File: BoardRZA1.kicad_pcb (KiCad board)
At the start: 4 copper layers, 85.5 x 79.9 mm, 158 parts, among them CON1 USB-MINI-B, CON2 USB-A-PCB, CON3 microSD, CON4 BARREL_JACK, J1 VGA, J2 SUPP32, K1 CONN_3, P1 CONN_5X2, P10 CONN_1, P11 CONN_1, P12 CONN_1, P13 CONN_1, P14 CONN_1, P15 CONN_1, P16 CONN_1, P17 CONN_1, P2 CONN_1, P3 CONN_1, P4 CONN_1, P5 CONN_1, P6 CONN_1, P7 CONN_1, P8 CONN_1, P9 CONN_1, SW1 RESET, SW2 NMI, SW3 SW0, SW4 SW1, U1 RZ-A1L, U2 13MHz, U3 48MHz, U4 N25QXXX, U5 AS4C16M16S, U6 BA3259HFP, U7 BU42xx, U8 TL074, X1 32.768k

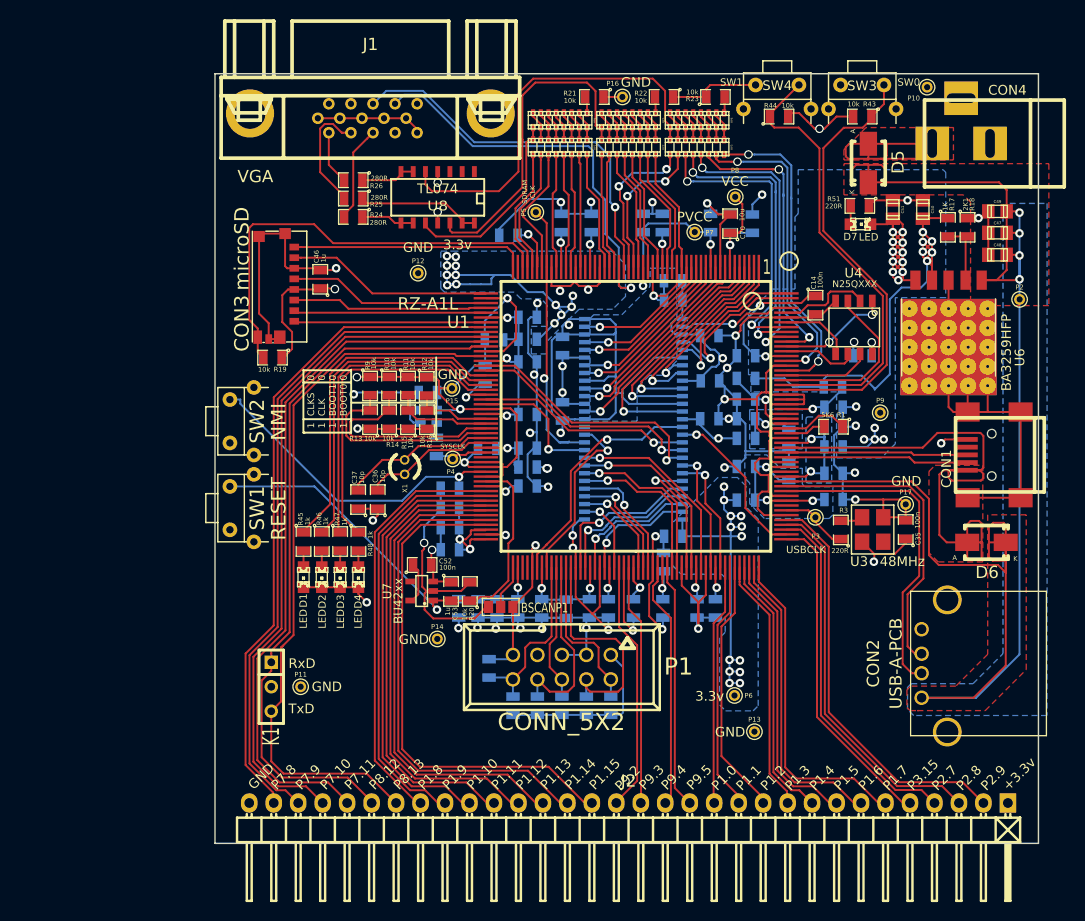
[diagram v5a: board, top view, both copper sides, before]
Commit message: Change R2R DAC for ADV7125 on LQFP48
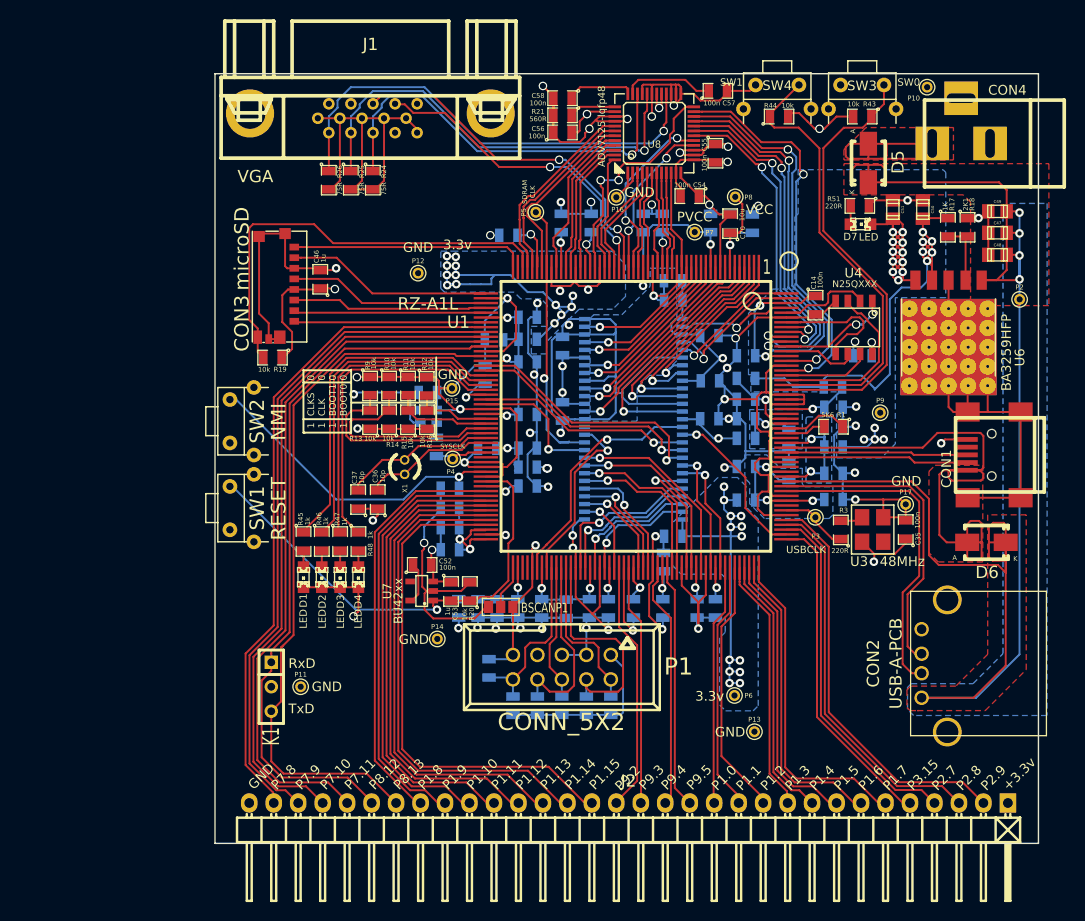
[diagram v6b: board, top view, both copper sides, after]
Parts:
- removed R22, R23: 10k, footprints:SM0805
- removed RP1, RP2, RP3: 20k, Resistors_SMD:r_cat16-8
- removed RP4, RP5, RP6: 10k, Resistors_SMD:r_cat16-8
- added C54: 100n, footprints:SM0805, F.Cu at (83.7, 30.4)
- added C55: 100n, footprints:SM0805, F.Cu at (86.4, 25.9)
- added C56: 100n, footprints:SM0805, F.Cu at (70.5, 23.7)
- added C57: 100n, footprints:SM0805, F.Cu at (86.6, 19.4)
- added C58: 100n, footprints:SM0805, F.Cu at (70.5, 20.2)
- R21: value 10k -> 560R
- R24, R25, R26: value 280R -> 75R
- U8: value TL074 -> ADV7125-lqfp48; footprint SMD_Packages:SO14E -> Housings_QFP:lqfp-48
- moved U8 23.5 mm to (80.0, 23.8), turned to 0 degrees
- moved P16 10.4 mm to (76.1, 30.5)
- moved R24 4.32 mm to (50.8, 28.7), turned to 270 degrees
- moved R21 3.81 mm to (70.5, 22.0)
- moved R26 2.54 mm to (46.2, 28.7), turned to 270 degrees
- moved R25 1.92 mm to (48.5, 28.7), turned to 270 degrees
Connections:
- J1 pad 1: Net-(J1-Pad1) -> /VGAB
- J1 pad 2: Net-(J1-Pad2) -> /VGAG
- J1 pad 3: Net-(J1-Pad3) -> /VGAR
- R21 pad 1: VSS -> Net-(R21-Pad1)
- R21 pad 2: Net-(R21-Pad2) -> VSS
- R24 pad 1: Net-(R24-Pad1) -> /VGAR
- R24 pad 2: Net-(J1-Pad3) -> VSS
- R25 pad 1: Net-(R25-Pad1) -> /VGAG
- R25 pad 2: Net-(J1-Pad2) -> VSS
- R26 pad 1: Net-(R26-Pad1) -> /VGAB
- R26 pad 2: Net-(J1-Pad1) -> VSS
- U1 pad 35: (no net) -> /LCD_PCLK
- U8 pad 1: (no net) -> VSS
- U8 pad 10: /VGA_B -> /LCD_DATA8
- U8 pad 11: VSS -> +3.3V
- U8 pad 12: /VGA_G -> VSS
- U8 pad 13: Net-(R25-Pad1) -> +3.3V
- U8 pad 14: Net-(R25-Pad1) -> VSS
- U8 pad 2: (no net) -> VSS
- U8 pad 3: (no net) -> /LCD_DATA15
- U8 pad 4: +3.3V -> /LCD_DATA14
- U8 pad 5: /VGA_R -> /LCD_DATA13
- U8 pad 6: Net-(R26-Pad1) -> /LCD_DATA12
- U8 pad 7: Net-(R26-Pad1) -> /LCD_DATA11
- U8 pad 8: Net-(R24-Pad1) -> /LCD_DATA10
- U8 pad 9: Net-(R24-Pad1) -> /LCD_DATA9
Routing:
- net VSS: track 566.0 -> 636.9 mm, vias 49 -> 56
- net /VGAB: track 0.00 -> 49.1 mm, vias 0 -> 1
- net /VGAG: track 0.00 -> 46.0 mm, vias 0 -> 1
- net /VGAR: track 0.00 -> 42.8 mm, vias 0 -> 1
- net /VGA_R: track 41.9 -> 0.00 mm
- net /VGA_G: track 34.5 -> 0.00 mm
- net /LCD_PCLK: track 0.00 -> 24.3 mm, vias 0 -> 2
- net /VGA_B: track 20.5 -> 0.00 mm
- net +3.3V: track 359.9 -> 377.8 mm, vias 50 -> 52
- net Net-(R25-Pad1): track 12.9 -> 0.00 mm
- net Net-(J1-Pad2): track 12.1 -> 0.00 mm
- net /LCD_DATA2: track 29.6 -> 40.0 mm
- net Net-(J1-Pad3): track 9.98 -> 0.00 mm
- net /LCD_VSYNC: track 43.1 -> 33.3 mm, vias 1 -> 2
- net Net-(C57-Pad1): track 0.00 -> 9.47 mm
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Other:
- net class Default: clearance 0.2032 -> 0.1778; trace_width 0.2032 -> 0.1778
- rule trace_clearance: 0.2032 -> 0.1778
- rule trace_min: 0.2032 -> 0.1778
